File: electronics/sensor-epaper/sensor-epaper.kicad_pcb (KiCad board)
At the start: 4 copper layers, 34 x 79.2 mm, 96 parts, among them J1 i2c, J2 Conn_01x06, J4 Display, J9 USB micro, Q1 Q_NMOS_GSD, Q2 NX2301P, Q3 NX2301P, SW1 SW_Push, U1 ESP32-C3FN4, U2 AMS1117-3.3, U3 NCP1421, U4 SHT40-AD1B-R2, Y2 32kHz, Y3 40MHz 10ppm

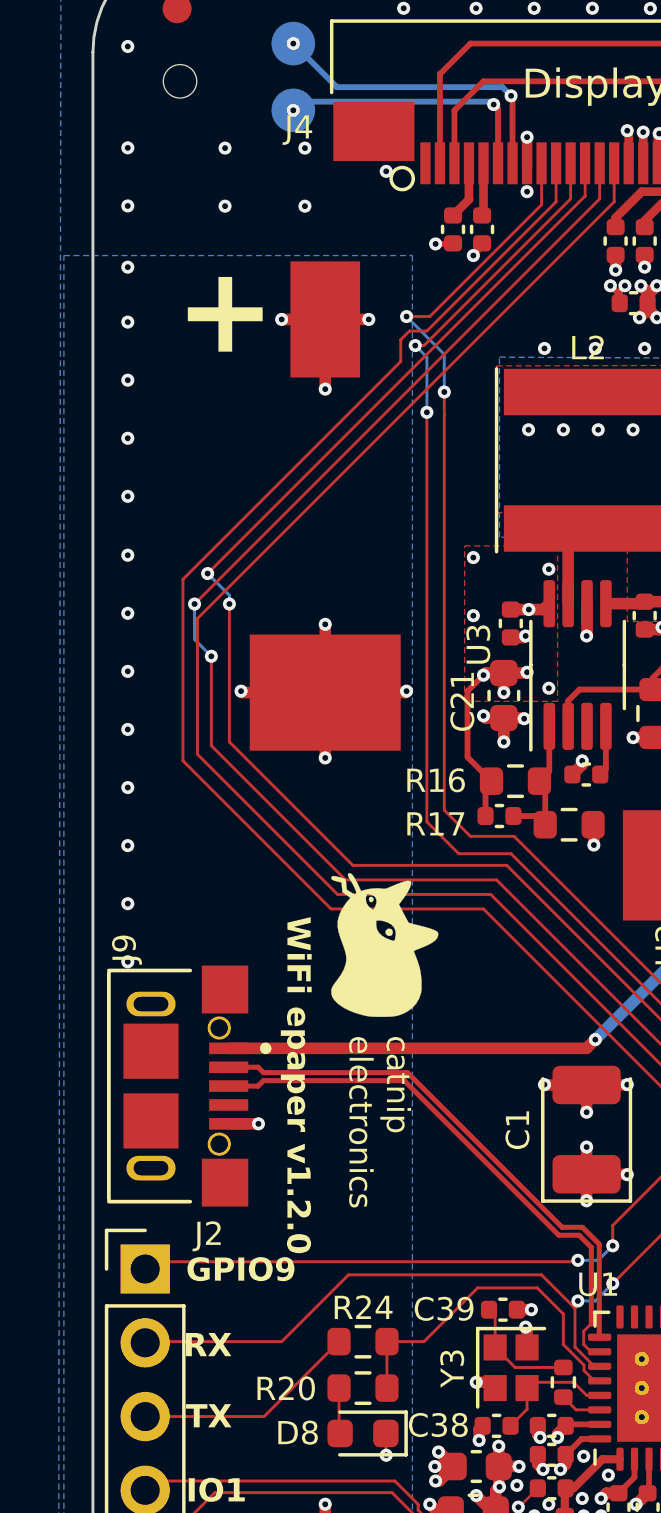
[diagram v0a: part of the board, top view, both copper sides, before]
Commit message: Add a silkscreen for git repo
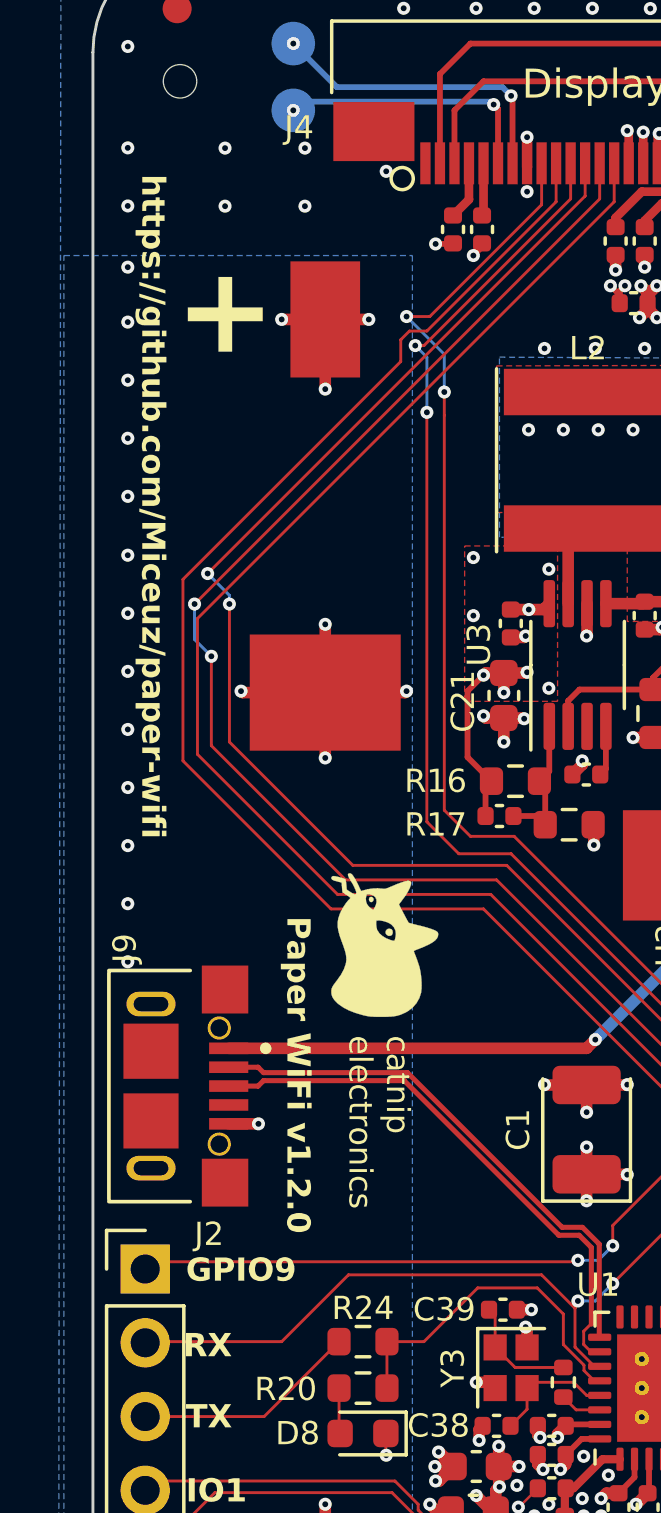
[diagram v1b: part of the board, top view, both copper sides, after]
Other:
- board text added: "Paper WiFi v1.2.0"
- board text added: "https://github.com/Miceuz/paper-wifi"
- board text removed: "WiFi epaper v1.2.0"
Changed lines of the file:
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@@
     (effects (font (size 0.8 0.8) (thickness 0.15) bold) (justify left bottom))
   )
-  (gr_text "WiFi epaper v1.2.0" (at 172.6 70.75 270) (layer "F.SilkS")
+  (gr_text "Paper WiFi v1.2.0" (at 172.6 70.75 270) (layer "F.SilkS")
     (effects (font (size 0.8 0.8) (thickness 0.15) bold) (justify left bottom))
   )
@@
     (effects (font (size 0.8 0.8) (thickness 0.15) bold) (justify left bottom))
   )
+  (gr_text "https://github.com/Miceuz/paper-wifi" (at 167.6 45.2 270) (layer "F.SilkS")
+    (effects (font (size 0.8 0.8) (thickness 0.15) bold) (justify left bottom))
+  )

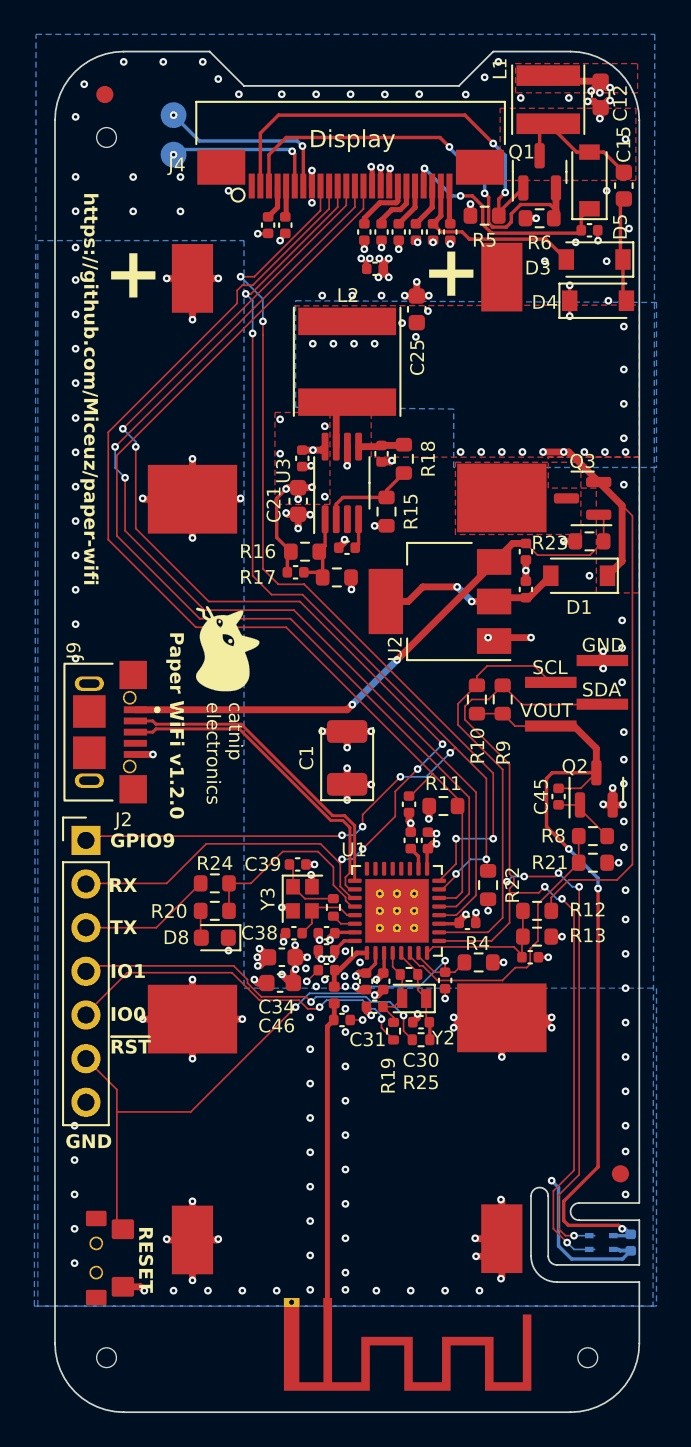
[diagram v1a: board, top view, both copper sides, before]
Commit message: Change DC/DC regulator to TPS61023 as previous one is out of stock. Change L1 and R6 to accomodate another display as previous one will be end of life soon
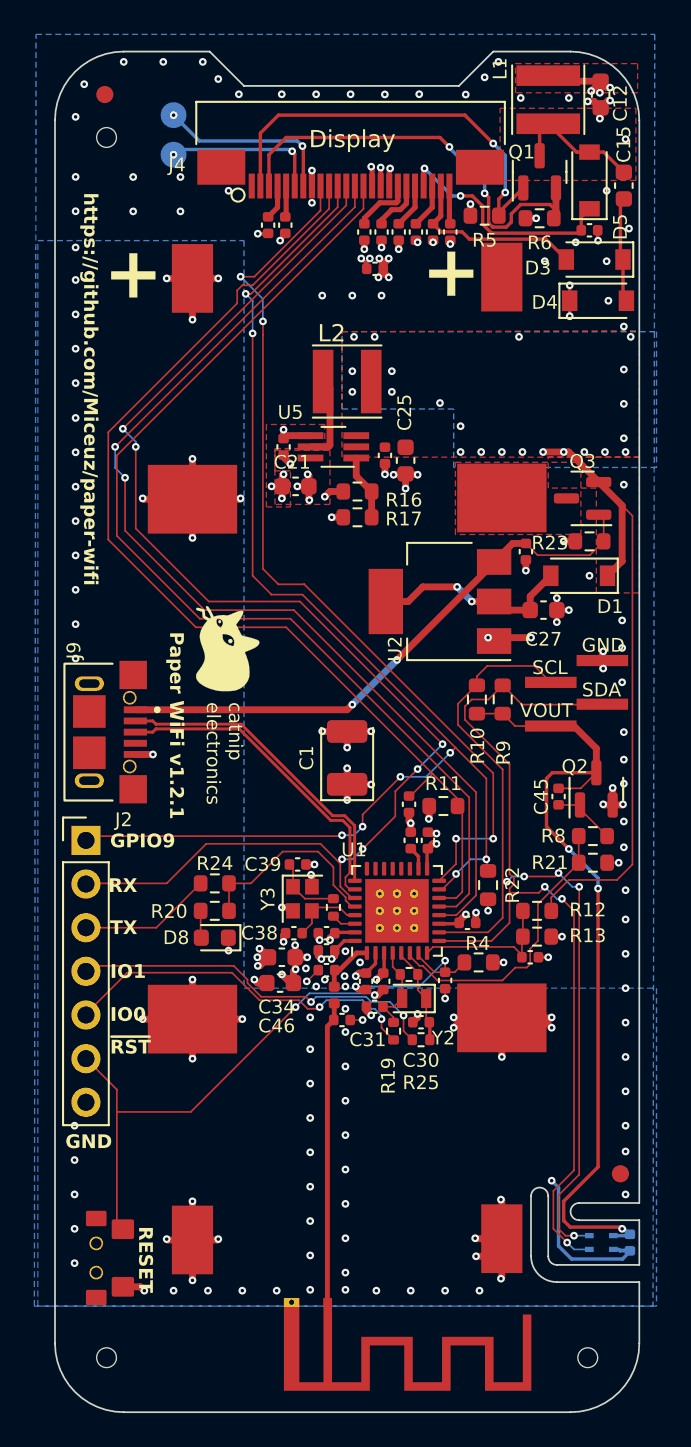
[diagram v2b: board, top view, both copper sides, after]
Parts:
- removed C42: 10p, Capacitor_SMD:C_0402_1005Metric
- removed C44: 1u, Capacitor_SMD:C_0402_1005Metric
- removed R15: 300k, Resistor_SMD:R_0603_1608Metric
- removed R18: 220k, Resistor_SMD:R_0603_1608Metric
- removed U3: NCP1421, Package_SO:MSOP-8_3x3mm_P0.65mm
- added U5: TPS61023, Package_TO_SOT_SMD:SOT-363_SC-70-6_Handsoldering, F.Cu at (182.2, 60.0)
- C27: value 1u -> 22u; footprint Capacitor_SMD:C_0402_1005Metric -> Capacitor_SMD:C_0603_1608Metric
- D1: value 1N4148 -> 2CZ4007
- L1: value 10u 1A -> 47u 0.5A
- L2: value 10u 1A -> 2u2 3A; footprint Inductor_SMD:L_Taiyo-Yuden_NR-60xx -> Inductor_SMD:L_Taiyo-Yuden_NR-40xx
- R6: value 0R47 -> 2R2
- moved C27 12.0 mm to (194.4, 69.5), turned to 0 degrees
- moved C25 8.82 mm to (186.4, 60.8), turned to -90 degrees
- moved R16 4.64 mm to (183.6, 62.6)
- moved R17 3.70 mm to (183.6, 64.1), turned to 180 degrees
- moved C22 1.28 mm to (179.3, 60.0), turned to 90 degrees
- moved L2 1.15 mm to (183.0, 56.2), turned to 180 degrees
- moved C21 0.86 mm to (180.0, 62.3), turned to 180 degrees
- moved C26 0.22 mm to (185.2, 60.5)
- moved C48 0.05 mm to (199.4, 106.3)
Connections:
- C27 pad 1: /REF_MAIN -> /USB_3V3
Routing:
- net /EN_MAIN: track 5.80 -> 0.00 mm
- net +3V3: track 41.7 -> 36.7 mm, vias 37 -> 34
- net /VIN: track 42.2 -> 39.7 mm, vias 16 -> 19
- net /SW_MAIN: track 2.85 -> 5.04 mm
- net /REF_MAIN: track 1.74 -> 0.00 mm
- net /USB_3V3: track 10.6 -> 11.8 mm
- net /FB_MAIN: track 4.83 -> 3.82 mm
- added copper zone on F.Cu, net GND
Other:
- board text added: "Paper WiFi v1.2.1"
- board text removed: "Paper WiFi v1.2.0"

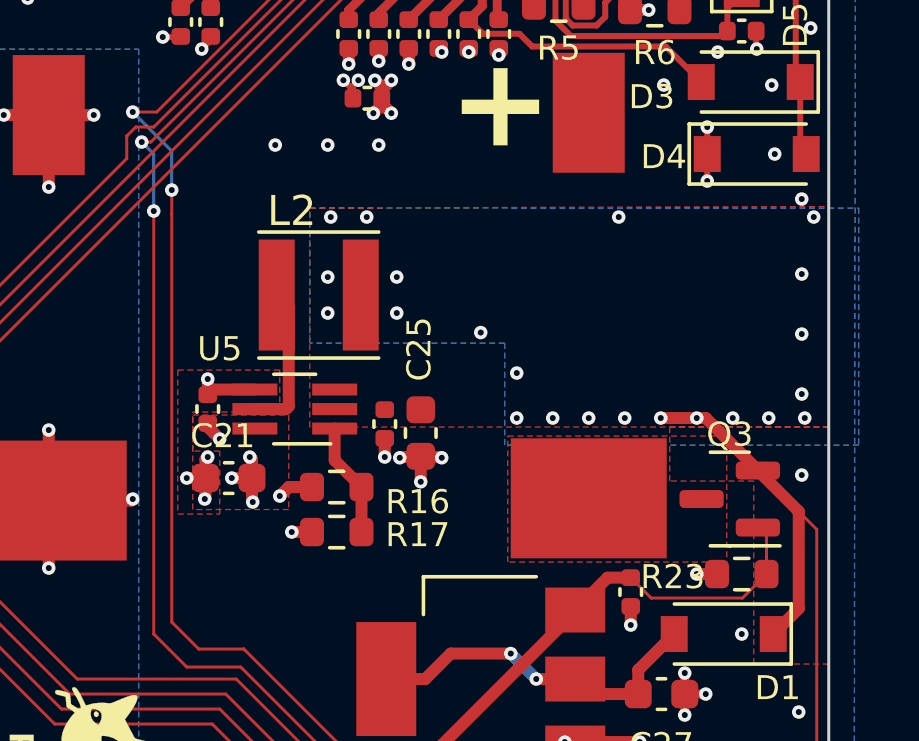
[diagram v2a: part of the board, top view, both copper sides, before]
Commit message: Put correct resistor into Dc/Dc converters divider. Fix SC70 footprint
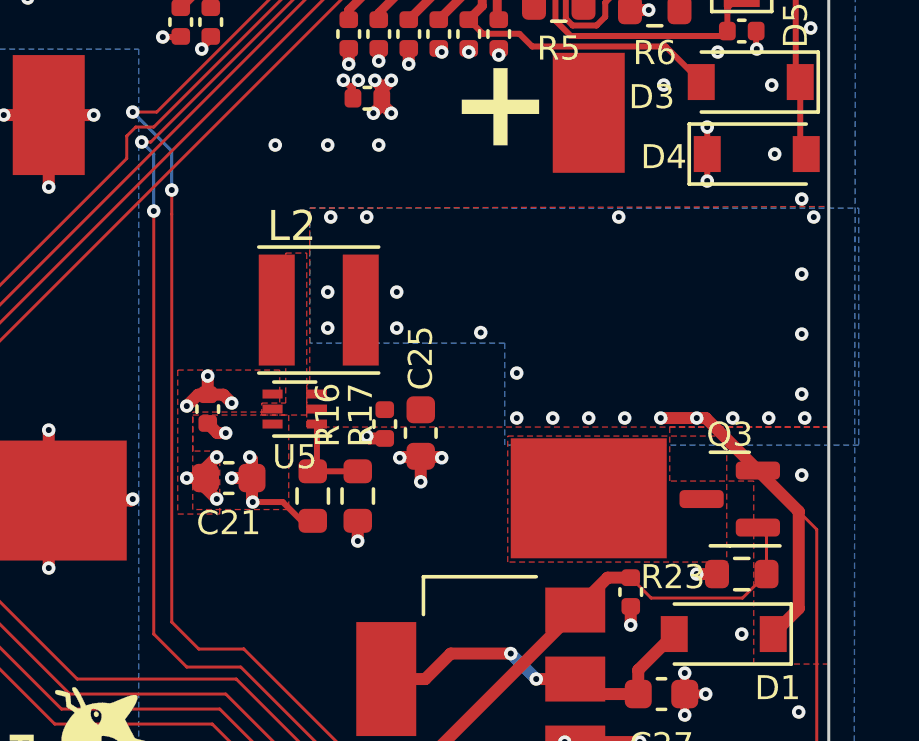
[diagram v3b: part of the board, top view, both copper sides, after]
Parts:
- R16: value 348k -> 931k
- U5: footprint Package_TO_SOT_SMD:SOT-363_SC-70-6_Handsoldering -> Package_TO_SOT_SMD:SOT-363_SC-70-6
- moved R17 1.39 mm to (184.3, 62.9), turned to -90 degrees
- moved R16 0.85 mm to (182.8, 62.9), turned to 90 degrees
- moved L2 0.50 mm to (183.0, 56.7)
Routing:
- net /SW_MAIN: track 5.04 -> 0.00 mm
- net +3V3: track 36.7 -> 37.8 mm, vias 34 -> 33
- net /FB_MAIN: track 3.82 -> 3.13 mm
- net GND: track 76.9 -> 77.5 mm, vias 186 -> 188
- added copper zone on F.Cu, net /SW_MAIN
